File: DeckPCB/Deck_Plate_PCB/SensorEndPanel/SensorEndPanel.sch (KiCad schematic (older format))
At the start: 1 part

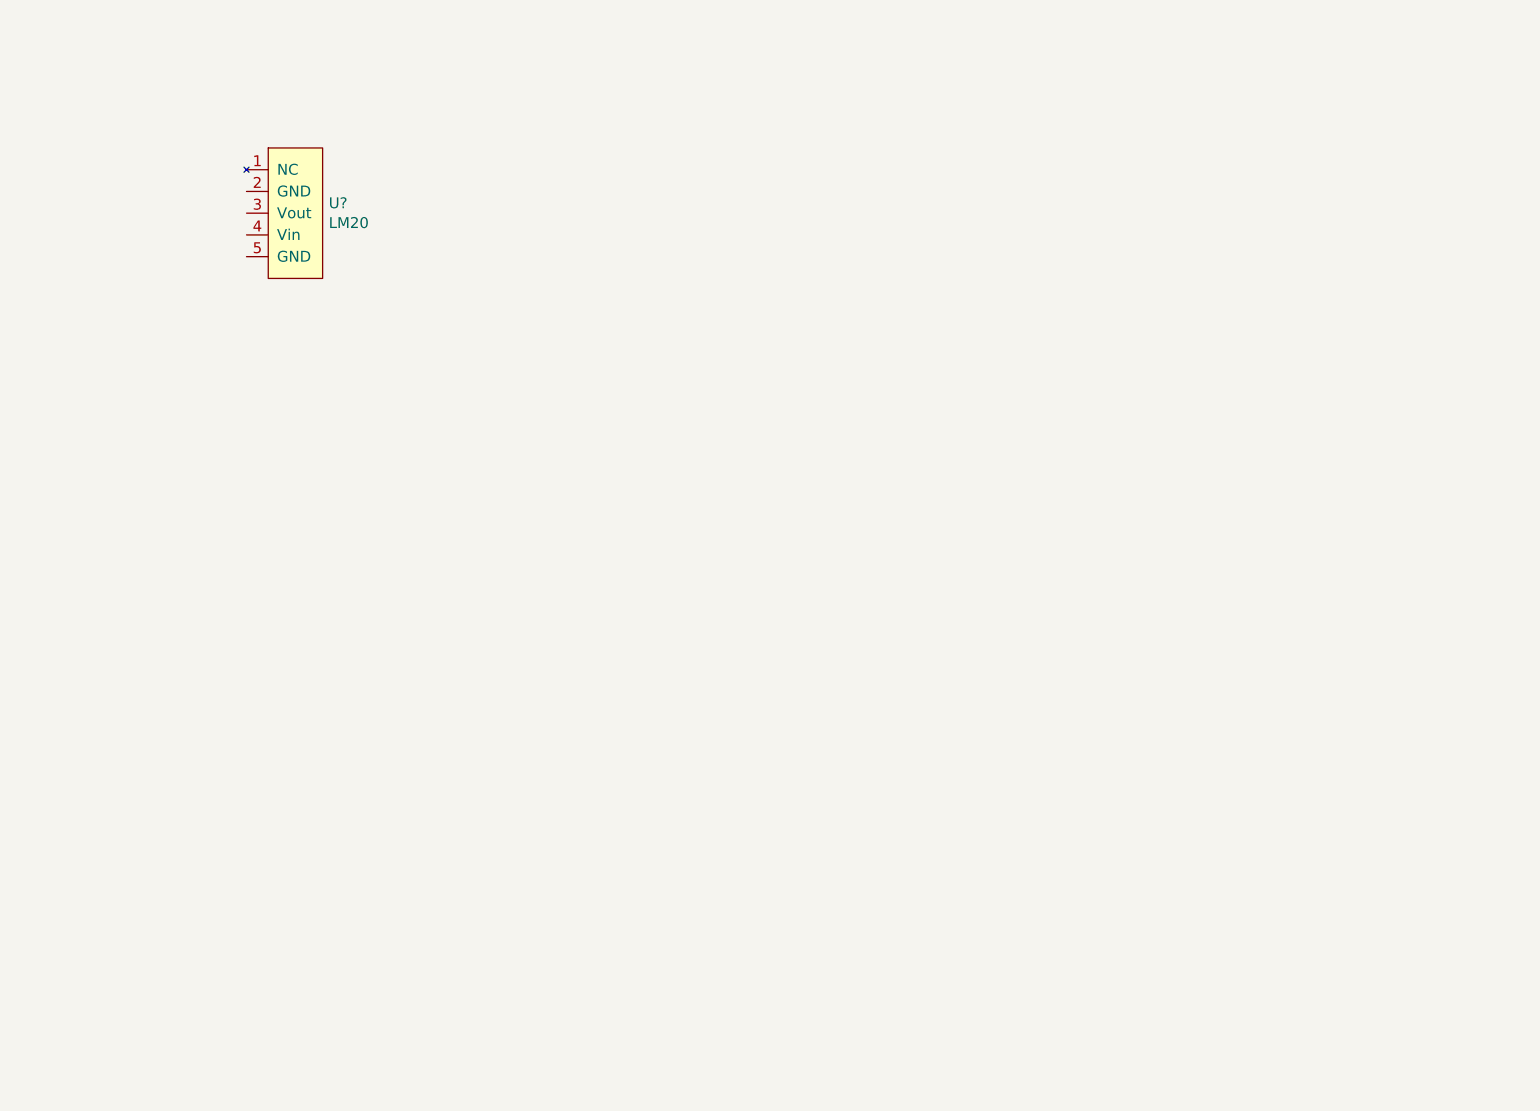
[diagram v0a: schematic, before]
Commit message: updated PCB routing and creation of BurnWire circuit board and updated Daughter_Board
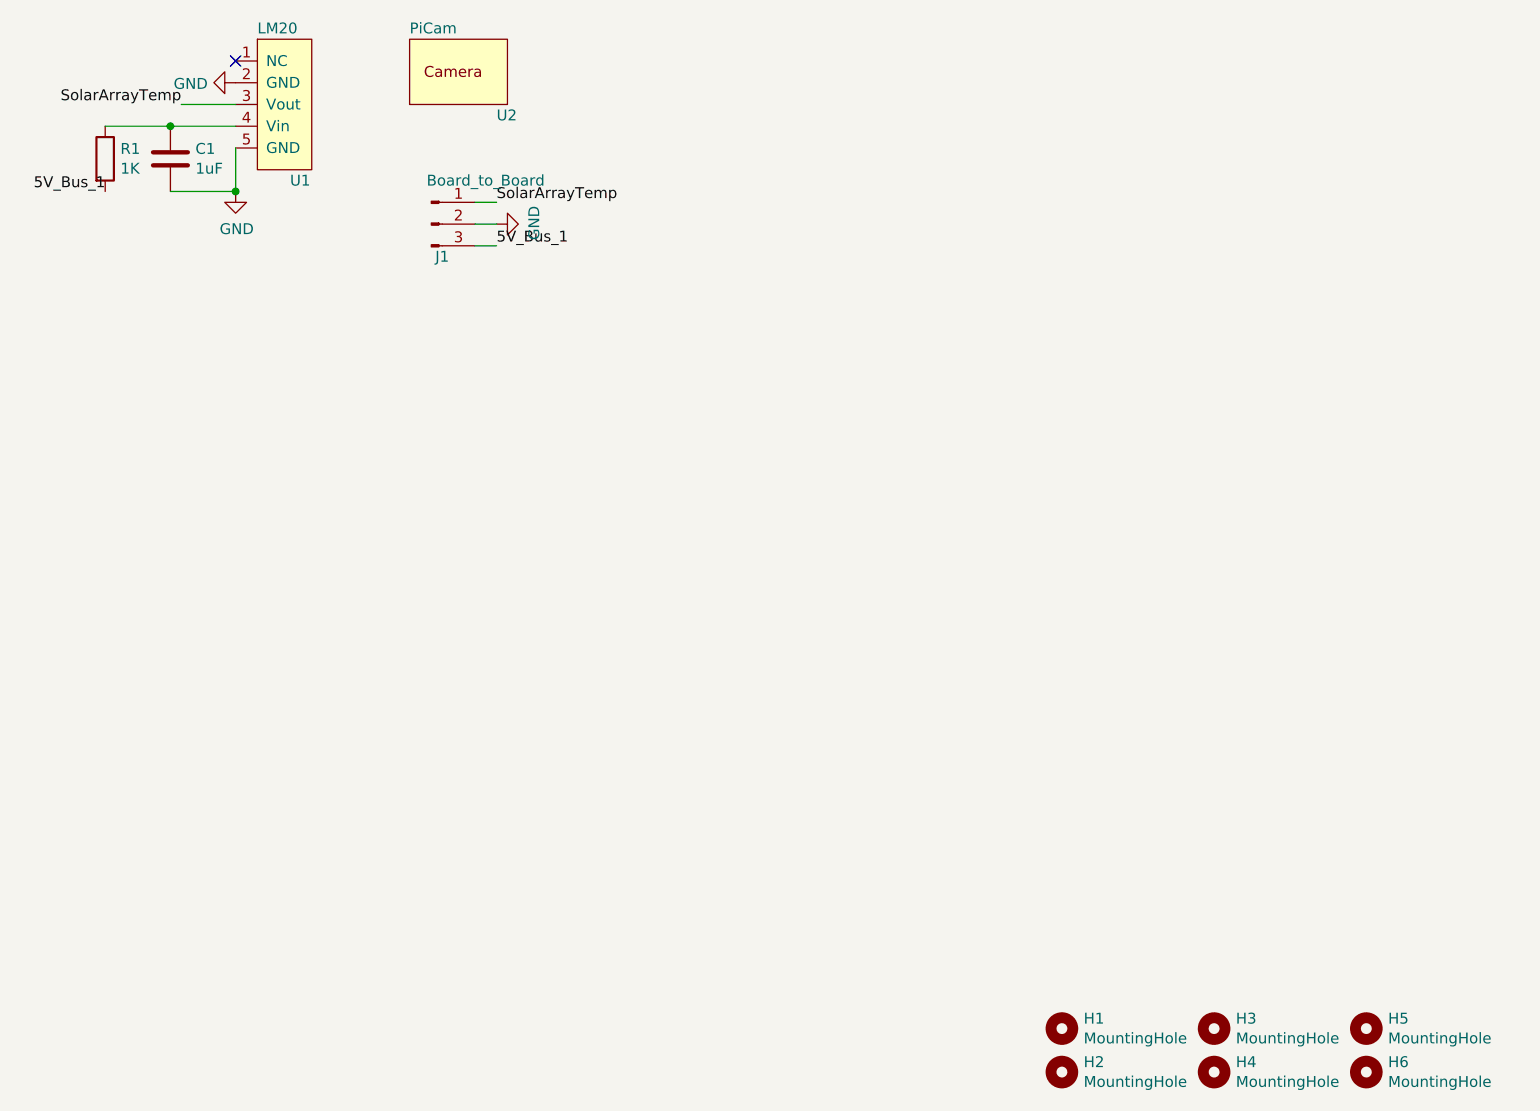
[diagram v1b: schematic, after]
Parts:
- added C1: 1uF, Capacitor_THT:C_Axial_L3.8mm_D2.6mm_P7.50mm_Horizontal, symbol Device:C
- added H1, H2, H3, H4, H5, H6: MountingHole, MountingHole:MountingHole_2mm, symbol Mechanical:MountingHole
- added J1: Board_to_Board, Connector_PinHeader_2.54mm:PinHeader_1x03_P2.54mm_Vertical, symbol Connector:Conn_01x03_Male
- added R1: 1K, Resistor_THT:R_Axial_DIN0207_L6.3mm_D2.5mm_P10.16mm_Horizontal, symbol Device:R
- added U2: PiCam, Deck_Plate_PCB:PiCam, symbol Deck_Plate_PCB:PiCam
- U1: renamed from U?; footprint (none) -> Package_TO_SOT_SMD:SOT-353_SC-70-5_Handsoldering
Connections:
- net GND: now reaches U1.2 (GND)
- net GND: now also U1.5 (GND), C1.2, J1.2 (Pin_2)
- net SolarArrayTemp: now reaches U1.3 (Vout)
- net SolarArrayTemp: now also J1.1 (Pin_1)
- net at U1.4 (Vin): now also C1.1, R1.1
- new net 5V_Bus_1: J1.3 (Pin_3), R1.2
- no-connect marks 0 -> 1
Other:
- moved on the sheet: U1
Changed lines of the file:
@@
 $EndDescr
 $Comp
-L Deck_Plate_PCB:LM20 U?
+L Deck_Plate_PCB:LM20 U1
 U 1 1 5E6E2023
-P 2750 2850
-F 0 "U?" H 3678 3346 50  0000 L CNN
-F 1 "LM20" H 3678 3255 50  0000 L CNN
-F 2 "" H 2850 3050 50  0001 C CNN
-F 3 "" H 2850 3050 50  0001 C CNN
-	1    2750 2850
+P 2700 2350
+F 0 "U1" H 3500 2450 50  0000 L CNN
+F 1 "LM20" H 3350 3150 50  0000 L CNN
+F 2 "Package_TO_SOT_SMD:SOT-353_SC-70-5_Handsoldering" H 2800 2550 50  0001 C CNN
+F 3 "" H 2800 2550 50  0001 C CNN
+	1    2700 2350
 	1    0    0    -1
 $EndComp
+$Comp
+L Deck_Plate_PCB:PiCam U2
+U 1 1 5E614F50
+P 4050 1900
+F 0 "U2" H 4450 1850 50  0000 L CNN
+F 1 "PiCam" H 4050 2250 50  0000 L CNN
+F 2 "Deck_Plate_PCB:PiCam" H 4050 1900 50  0001 C CNN
+F 3 "" H 4050 1900 50  0001 C CNN
+	1    4050 1900
+	1    0    0    -1
+$EndComp
+NoConn ~ 3250 1700
+$Comp
+L power:GND #PWR0101
+U 1 1 5E615413
+P 3250 1800
+F 0 "#PWR0101" H 3250 1550 50  0001 C CNN
+F 1 "GND" V 3255 1672 50  0000 R CNN
+F 2 "" H 3250 1800 50  0001 C CNN
+F 3 "" H 3250 1800 50  0001 C CNN
+	1    3250 1800
+	0    1    1    0
+$EndComp
+Wire Wire Line
+	3250 2000 2950 2000
+$Comp
+L Device:R R1
+U 1 1 5E615BC7
+P 2650 2150
+F 0 "R1" H 2720 2196 50  0000 L CNN
+F 1 "1K" H 2720 2105 50  0000 L CNN
+F 2 "Resistor_THT:R_Axial_DIN0207_L6.3mm_D2.5mm_P10.16mm_Horizontal" V 2580 2150 50  0001 C CNN
+F 3 "~" H 2650 2150 50  0001 C CNN
+	1    2650 2150
+	1    0    0    -1
+$EndComp
+$Comp
+L Device:C C1
+U 1 1 5E6165D4
+P 2950 2150
+F 0 "C1" H 3065 2196 50  0000 L CNN
+F 1 "1uF" H 3065 2105 50  0000 L CNN
+F 2 "Capacitor_THT:C_Axial_L3.8mm_D2.6mm_P7.50mm_Horizontal" H 2988 2000 50  0001 C CNN
+F 3 "~" H 2950 2150 50  0001 C CNN
+	1    2950 2150
+	1    0    0    -1
+$EndComp
+Connection ~ 2950 2000
+Wire Wire Line
+	2650 2000 2950 2000
+$Comp
+L power:GND #PWR0102
+U 1 1 5E616F5F
+P 3250 2300
+F 0 "#PWR0102" H 3250 2050 50  0001 C CNN
+F 1 "GND" H 3255 2127 50  0000 C CNN
+F 2 "" H 3250 2300 50  0001 C CNN
+F 3 "" H 3250 2300 50  0001 C CNN
+	1    3250 2300
+	1    0    0    -1
+$EndComp
+Wire Wire Line
+	2950 2300 3250 2300
+Wire Wire Line
+	3250 2100 3250 2300
+Connection ~ 3250 2300
+Text Label 2650 2300 2    50   ~ 0
+5V_Bus_1
+Wire Wire Line
+	3250 1900 3000 1900
+Text Label 3000 1900 2    50   ~ 0
+SolarArrayTemp
+$Comp
+L Connector:Conn_01x03_Male J1
+U 1 1 5E61A4CE
+P 4150 2450
+F 0 "J1" H 4200 2300 50  0000 C CNN
+F 1 "Board_to_Board" H 4400 2650 50  0000 C CNN
+F 2 "Connector_PinHeader_2.54mm:PinHeader_1x03_P2.54mm_Vertical" H 4150 2450 50  0001 C CNN
+F 3 "~" H 4150 2450 50  0001 C CNN
+	1    4150 2450
+	1    0    0    -1
+$EndComp
+Wire Wire Line
+	4350 2350 4450 2350
+Wire Wire Line
+	4350 2450 4450 2450
+Wire Wire Line
+	4350 2550 4450 2550
+Text Label 4450 2550 0    50   ~ 0
+5V_Bus_1
+$Comp
+L power:GND #PWR0103
+U 1 1 5E61ADE9
+P 4450 2450
+F 0 "#PWR0103" H 4450 2200 50  0001 C CNN
+F 1 "GND" H 4455 2277 50  0000 C CNN
+F 2 "" H 4450 2450 50  0001 C CNN
+F 3 "" H 4450 2450 50  0001 C CNN
+	1    4450 2450
+	0    -1   -1   0
+$EndComp
+Text Label 4450 2350 0    50   ~ 0
+SolarArrayTemp
+$Comp
+L Mechanical:MountingHole H2
+U 1 1 5E61D2B4
+P 7050 6350
+F 0 "H2" H 7150 6396 50  0000 L CNN
+F 1 "MountingHole" H 7150 6305 50  0000 L CNN
+F 2 "MountingHole:MountingHole_2mm" H 7050 6350 50  0001 C CNN
+F 3 "~" H 7050 6350 50  0001 C CNN
+	1    7050 6350
+	1    0    0    -1
+$EndComp
+$Comp
+L Mechanical:MountingHole H1
+U 1 1 5E61D9B6
+P 7050 6150
+F 0 "H1" H 7150 6196 50  0000 L CNN
+F 1 "MountingHole" H 7150 6105 50  0000 L CNN
+F 2 "MountingHole:MountingHole_2mm" H 7050 6150 50  0001 C CNN
+F 3 "~" H 7050 6150 50  0001 C CNN
+	1    7050 6150
+	1    0    0    -1
+$EndComp
+$Comp
+L Mechanical:MountingHole H3
+U 1 1 5E61DC34
+P 7750 6150
+F 0 "H3" H 7850 6196 50  0000 L CNN
+F 1 "MountingHole" H 7850 6105 50  0000 L CNN
+F 2 "MountingHole:MountingHole_2mm" H 7750 6150 50  0001 C CNN
+F 3 "~" H 7750 6150 50  0001 C CNN
+	1    7750 6150
+	1    0    0    -1
+$EndComp
+$Comp
+L Mechanical:MountingHole H4
+U 1 1 5E61DDCA
+P 7750 6350
+F 0 "H4" H 7850 6396 50  0000 L CNN
+F 1 "MountingHole" H 7850 6305 50  0000 L CNN
+F 2 "MountingHole:MountingHole_2mm" H 7750 6350 50  0001 C CNN
+F 3 "~" H 7750 6350 50  0001 C CNN
+	1    7750 6350
+	1    0    0    -1
+$EndComp
+$Comp
+L Mechanical:MountingHole H6
+U 1 1 5E61E00F
+P 8450 6350
+F 0 "H6" H 8550 6396 50  0000 L CNN
+F 1 "MountingHole" H 8550 6305 50  0000 L CNN
+F 2 "MountingHole:MountingHole_2mm" H 8450 6350 50  0001 C CNN
+F 3 "~" H 8450 6350 50  0001 C CNN
+	1    8450 6350
+	1    0    0    -1
+$EndComp
+$Comp
+L Mechanical:MountingHole H5
+U 1 1 5E61E338
+P 8450 6150
+F 0 "H5" H 8550 6196 50  0000 L CNN
+F 1 "MountingHole" H 8550 6105 50  0000 L CNN
+F 2 "MountingHole:MountingHole_2mm" H 8450 6150 50  0001 C CNN
+F 3 "~" H 8450 6150 50  0001 C CNN
+	1    8450 6150
+	1    0    0    -1
+$EndComp
